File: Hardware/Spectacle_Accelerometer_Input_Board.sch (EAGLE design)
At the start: 45 parts, among them J2 FTDI_DEVICE, J3 AUDIO-JACK3, J4 AUDIO-JACK3, U1 CY8C4146LQI-S422, U2 3.3V/150mA, U3 ADXL345

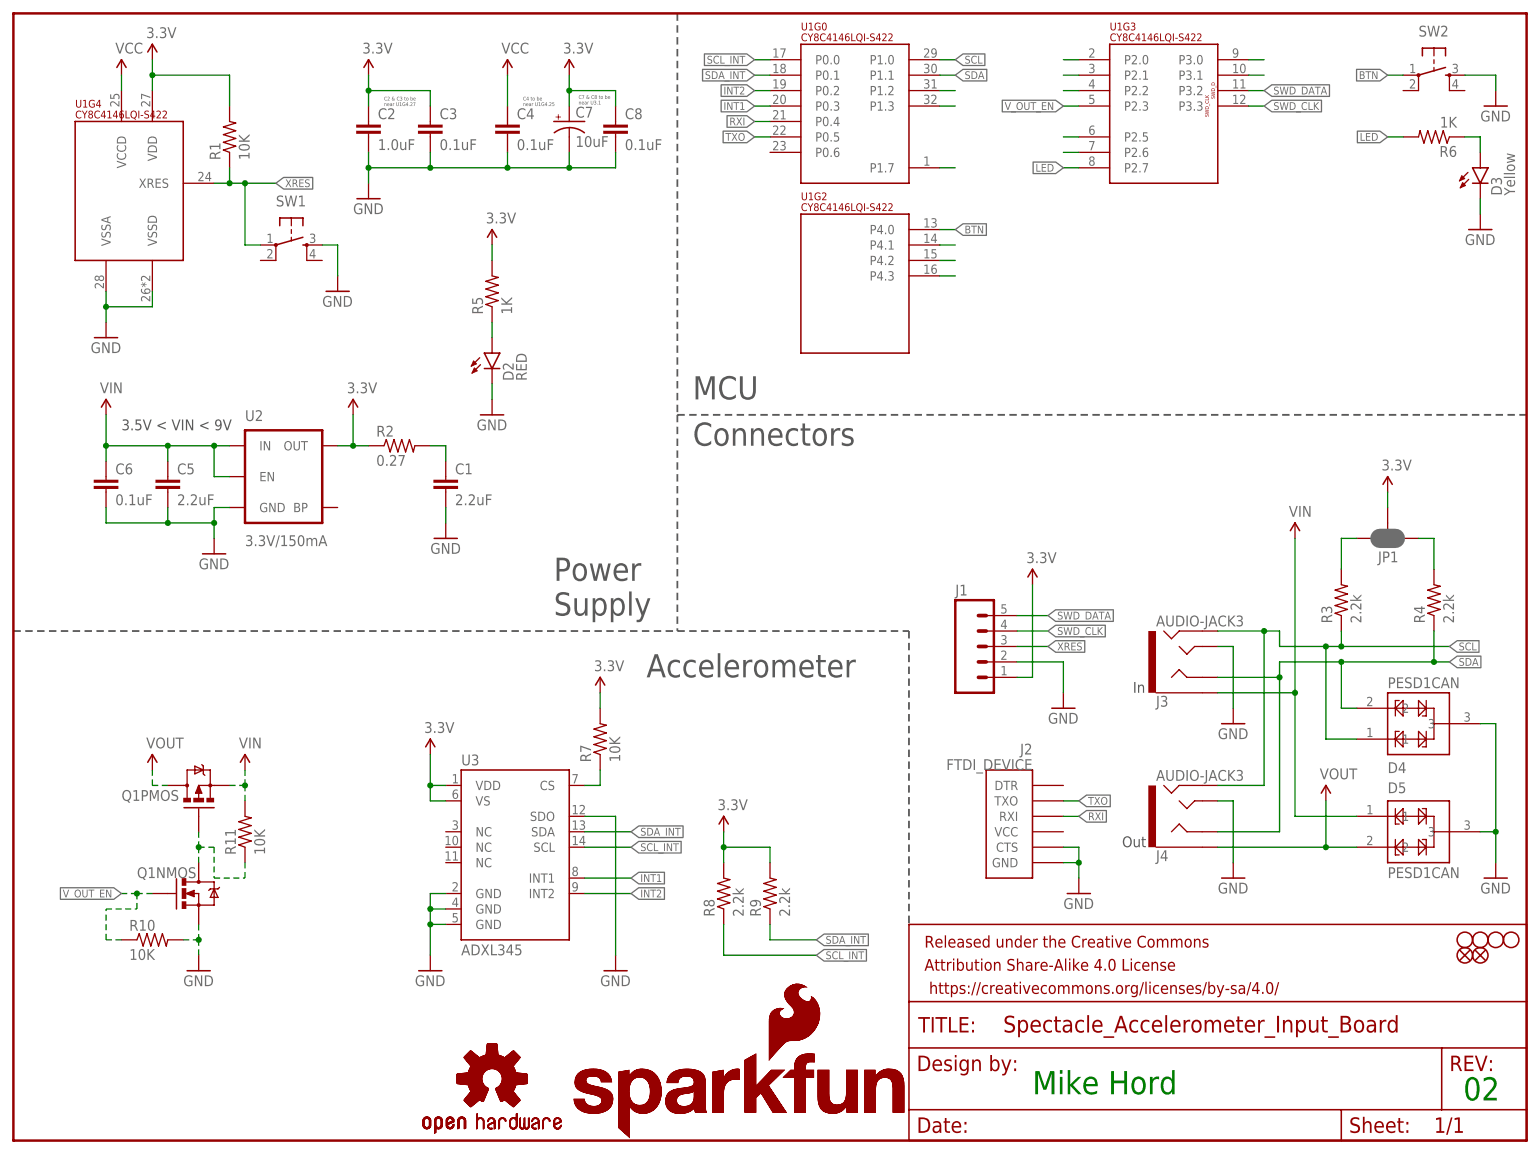
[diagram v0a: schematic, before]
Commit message: I2C disconnect circuitry added
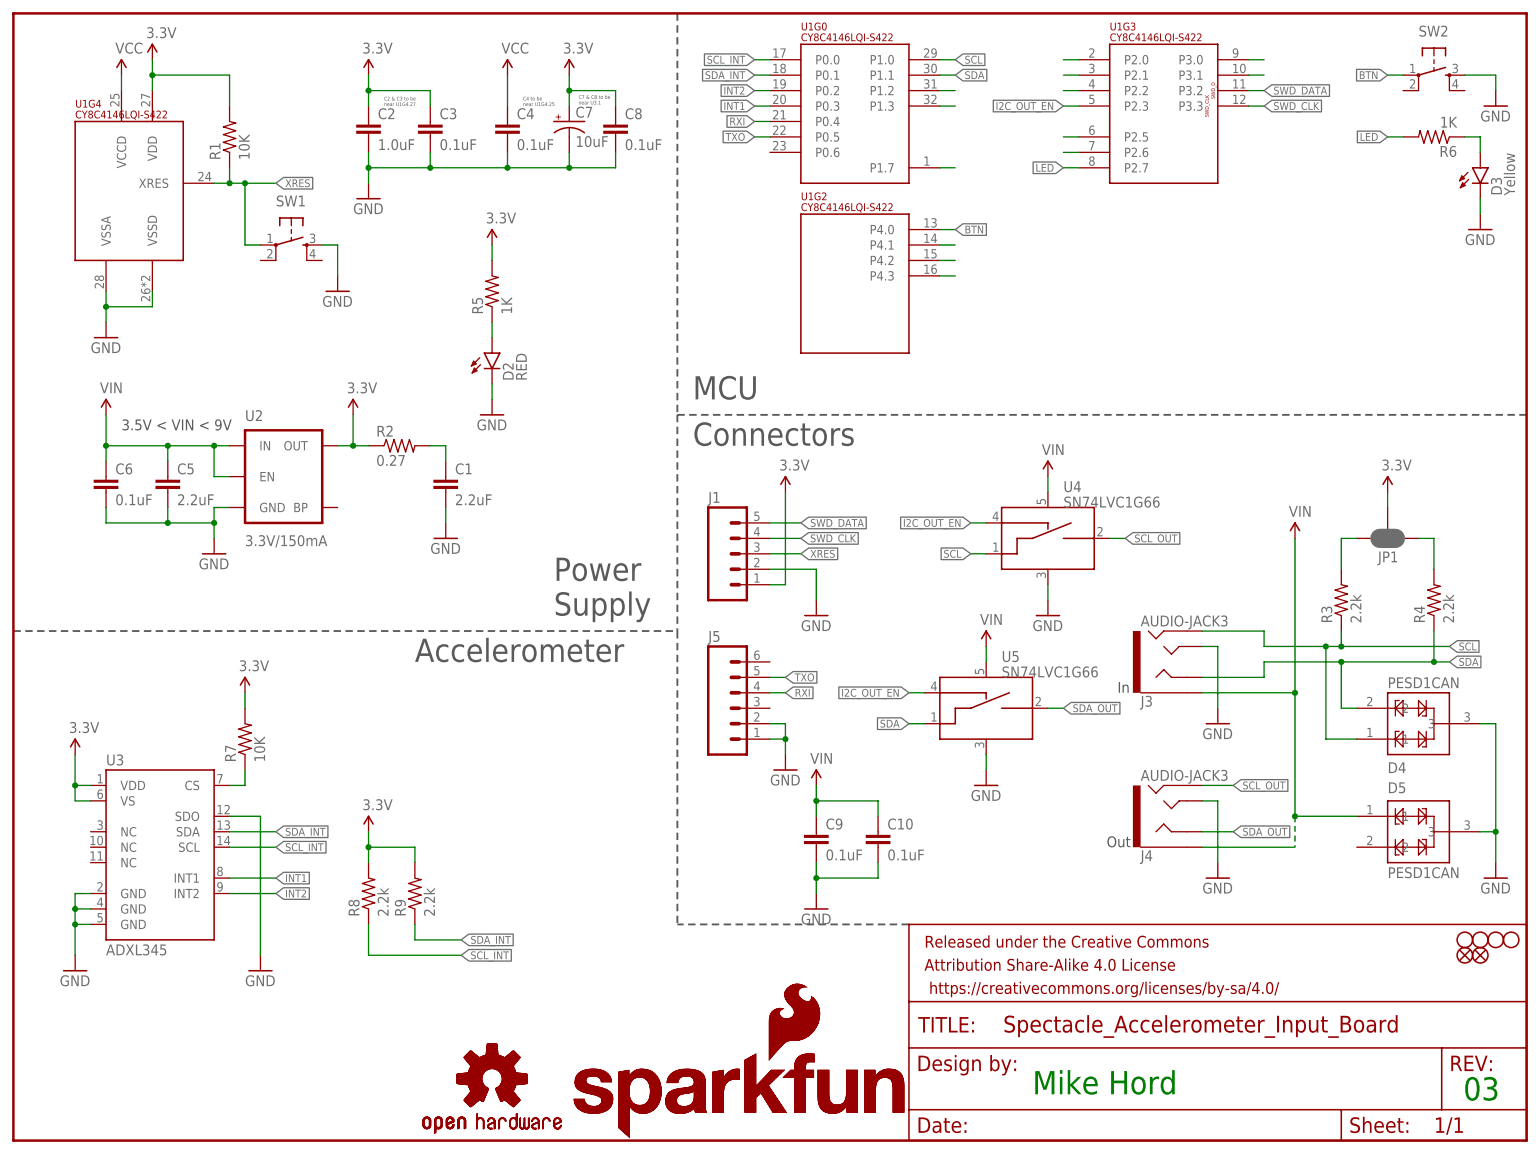
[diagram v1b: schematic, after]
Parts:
- removed J2: FTDI_DEVICE, SparkFun-Connectors:FTDI_DEVICE
- removed Q1: (no value), SparkFun-DiscreteSemi:IRF7509
- removed R10, R11: 10K, SparkFun-Resistors:10KOHM-1/10W-1%(0603)0603
- added C10, C9: 0.1uF, SparkFun-Capacitors:0.1UF-16V(+-10%)(0402)
- added J5: (no value), SparkFun-Connectors:M06NO_SILK_FEMALE_PTH
- added U4, U5: SN74LVC1G66, SparkFun-AnalogIC:SN74LVC1G66_SPST_AMUX
- J1: device SparkFun-Connectors:M05PTH -> SparkFun-Connectors:M05NO_SILK
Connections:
- removed net N$37: Q1NMOS.D, Q1PMOS.G, R11.1
- removed net VOUT: D5.2, J4.EARTH, Q1PMOS.D
- removed net V_OUT_EN: Q1NMOS.G, R10.1, U1G3.P2.3
- new net I2C_OUT_EN: U1G3.P2.3, U4.CTRL_IN, U5.CTRL_IN
- new net SCL_OUT: J4.RING2, U4.A_OUT
- new net SDA_OUT: J4.RING1, U5.A_OUT
- net GND: now also C10.2, C9.2, J5.1, J5.2, U4.VSS, U5.VSS; no longer J2.CTS, J2.GND, Q1NMOS.S, R10.2
- net RXI: now also J5.4; no longer J2.RXI
- net SCL: now also U4.A_IN; no longer J4.RING2
- net SDA: now also U5.A_IN; no longer J4.RING1
- net TXO: now also J5.5; no longer J2.TXO
- net VIN: now also C10.1, C9.1, J4.EARTH, U4.VCC, U5.VCC; no longer Q1PMOS.S, R11.2
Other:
- note added: "03"
- note removed: "02"
- moved on the sheet: J1, J3, J4, R7, R8, R9, U3

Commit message: Change 2.2k I2C pullup to 4.7k Add Arduino test sketch
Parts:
- R3, R4, R8, R9: value 2.2k -> 4.7K; device SparkFun-Resistors:2.2KOHM-1/10W-1%(0603) -> SparkFun-Resistors:4.7KOHM-1/10W-1%(0603)
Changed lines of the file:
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@@
 <grid distance="0.1" unitdist="inch" unit="inch" style="lines" multiple="1" display="no" altdistance="0.01" altunitdist="inch" altunit="inch"/>
 <layers>
-<layer number="1" name="Top" color="4" fill="1" visible="yes" active="no"/>
-<layer number="2" name="Route2" color="1" fill="3" visible="yes" active="no"/>
-<layer number="3" name="Route3" color="4" fill="3" visible="yes" active="no"/>
-<layer number="4" name="Route4" color="1" fill="4" visible="yes" active="no"/>
-<layer number="5" name="Route5" color="4" fill="4" visible="yes" active="no"/>
-<layer number="6" name="Route6" color="1" fill="8" visible="yes" active="no"/>
-<layer number="7" name="Route7" color="4" fill="8" visible="yes" active="no"/>
-<layer number="8" name="Route8" color="1" fill="2" visible="yes" active="no"/>
-<layer number="9" name="Route9" color="4" fill="2" visible="yes" active="no"/>
-<layer number="10" name="Route10" color="1" fill="7" visible="yes" active="no"/>
-<layer number="11" name="Route11" color="4" fill="7" visible="yes" active="no"/>
-<layer number="12" name="Route12" color="1" fill="5" visible="yes" active="no"/>
-<layer number="13" name="Route13" color="4" fill="5" visible="yes" active="no"/>
-<layer number="14" name="Route14" color="1" fill="6" visible="yes" active="no"/>
-<layer number="15" name="Route15" color="4" fill="6" visible="yes" active="no"/>
-<layer number="16" name="Bottom" color="1" fill="1" visible="yes" active="no"/>
-<layer number="17" name="Pads" color="2" fill="1" visible="yes" active="no"/>
-<layer number="18" name="Vias" color="2" fill="1" visible="yes" active="no"/>
-<layer number="19" name="Unrouted" color="6" fill="1" visible="yes" active="no"/>
-<layer number="20" name="Dimension" color="15" fill="1" visible="yes" active="no"/>
-<layer number="21" name="tPlace" color="16" fill="1" visible="yes" active="no"/>
-<layer number="22" name="bPlace" color="14" fill="1" visible="yes" active="no"/>
-<layer number="23" name="tOrigins" color="15" fill="1" visible="yes" active="no"/>
-<layer number="24" name="bOrigins" color="15" fill="1" visible="yes" active="no"/>
-<layer number="25" name="tNames" color="7" fill="1" visible="yes" active="no"/>
-<layer number="26" name="bNames" color="7" fill="1" visible="yes" active="no"/>
-<layer number="27" name="tValues" color="7" fill="1" visible="yes" active="no"/>
-<layer number="28" name="bValues" color="7" fill="1" visible="yes" active="no"/>
+<layer number="1" name="Top" color="4" fill="1" visible="no" active="no"/>
+<layer number="2" name="Route2" color="1" fill="3" visible="no" active="no"/>
+<layer number="3" name="Route3" color="4" fill="3" visible="no" active="no"/>
+<layer number="4" name="Route4" color="1" fill="4" visible="no" active="no"/>
+<layer number="5" name="Route5" color="4" fill="4" visible="no" active="no"/>
+<layer number="6" name="Route6" color="1" fill="8" visible="no" active="no"/>
+<layer number="7" name="Route7" color="4" fill="8" visible="no" active="no"/>
+<layer number="8" name="Route8" color="1" fill="2" visible="no" active="no"/>
+<layer number="9" name="Route9" color="4" fill="2" visible="no" active="no"/>
+<layer number="10" name="Route10" color="1" fill="7" visible="no" active="no"/>
+<layer number="11" name="Route11" color="4" fill="7" visible="no" active="no"/>
+<layer number="12" name="Route12" color="1" fill="5" visible="no" active="no"/>
+<layer number="13" name="Route13" color="4" fill="5" visible="no" active="no"/>
+<layer number="14" name="Route14" color="1" fill="6" visible="no" active="no"/>
+<layer number="15" name="Route15" color="4" fill="6" visible="no" active="no"/>
+<layer number="16" name="Bottom" color="1" fill="1" visible="no" active="no"/>
+<layer number="17" name="Pads" color="2" fill="1" visible="no" active="no"/>
+<layer number="18" name="Vias" color="2" fill="1" visible="no" active="no"/>
+<layer number="19" name="Unrouted" color="6" fill="1" visible="no" active="no"/>
+<layer number="20" name="Dimension" color="15" fill="1" visible="no" active="no"/>
+<layer number="21" name="tPlace" color="16" fill="1" visible="no" active="no"/>
+<layer number="22" name="bPlace" color="14" fill="1" visible="no" active="no"/>
+<layer number="23" name="tOrigins" color="15" fill="1" visible="no" active="no"/>
+<layer number="24" name="bOrigins" color="15" fill="1" visible="no" active="no"/>
+<layer number="25" name="tNames" color="7" fill="1" visible="no" active="no"/>
+<layer number="26" name="bNames" color="7" fill="1" visible="no" active="no"/>
+<layer number="27" name="tValues" color="7" fill="1" visible="no" active="no"/>
+<layer number="28" name="bValues" color="7" fill="1" visible="no" active="no"/>
 <layer number="29" name="tStop" color="7" fill="3" visible="no" active="no"/>
 <layer number="30" name="bStop" color="7" fill="6" visible="no" active="no"/>
@@
 <layer number="35" name="tGlue" color="7" fill="4" visible="no" active="no"/>
 <layer number="36" name="bGlue" color="7" fill="5" visible="no" active="no"/>
-<layer number="37" name="tTest" color="7" fill="1" visible="yes" active="no"/>
-<layer number="38" name="bTest" color="7" fill="1" visible="yes" active="no"/>
+<layer number="37" name="tTest" color="7" fill="1" visible="no" active="no"/>
+<layer number="38" name="bTest" color="7" fill="1" visible="no" active="no"/>
 <layer number="39" name="tKeepout" color="4" fill="11" visible="no" active="no"/>
 <layer number="40" name="bKeepout" color="1" fill="11" visible="no" active="no"/>
@@
 <layer number="44" name="Drills" color="7" fill="1" visible="no" active="no"/>
 <layer number="45" name="Holes" color="7" fill="1" visible="no" active="no"/>
-<layer number="46" name="Milling" color="3" fill="1" visible="yes" active="no"/>
-<layer number="47" name="Measures" color="7" fill="1" visible="yes" active="no"/>
-<layer number="48" name="Document" color="7" fill="1" visible="yes" active="no"/>
-<layer number="49" name="Reference" color="7" fill="1" visible="yes" active="no"/>
-<layer number="50" name="dxf" color="7" fill="1" visible="yes" active="no"/>
-<layer number="51" name="tDocu" color="6" fill="1" visible="yes" active="no"/>
-<layer number="52" name="bDocu" color="7" fill="1" visible="yes" active="no"/>
-<layer number="53" name="tGND_GNDA" color="7" fill="9" visible="yes" active="no"/>
-<layer number="54" name="bGND_GNDA" color="1" fill="9" visible="yes" active="no"/>
-<layer number="56" name="wert" color="7" fill="1" visible="yes" active="no"/>
-<layer number="57" name="tCAD" color="7" fill="1" visible="yes" active="no"/>
-<layer number="59" name="tCarbon" color="7" fill="1" visible="yes" active="no"/>
-<layer number="60" name="bCarbon" color="7" fill="1" visible="yes" active="no"/>
+<layer number="46" name="Milling" color="3" fill="1" visible="no" active="no"/>
+<layer number="47" name="Measures" color="7" fill="1" visible="no" active="no"/>
+<layer number="48" name="Document" color="7" fill="1" visible="no" active="no"/>
+<layer number="49" name="Reference" color="7" fill="1" visible="no" active="no"/>
+<layer number="50" name="dxf" color="7" fill="1" visible="no" active="no"/>
+<layer number="51" name="tDocu" color="6" fill="1" visible="no" active="no"/>
+<layer number="52" name="bDocu" color="7" fill="1" visible="no" active="no"/>
+<layer number="53" name="tGND_GNDA" color="7" fill="9" visible="no" active="no"/>
+<layer number="54" name="bGND_GNDA" color="1" fill="9" visible="no" active="no"/>
+<layer number="56" name="wert" color="7" fill="1" visible="no" active="no"/>
+<layer number="57" name="tCAD" color="7" fill="1" visible="no" active="no"/>
+<layer number="59" name="tCarbon" color="7" fill="1" visible="no" active="no"/>
+<layer number="60" name="bCarbon" color="7" fill="1" visible="no" active="no"/>
 <layer number="90" name="Modules" color="5" fill="1" visible="yes" active="yes"/>
 <layer number="91" name="Nets" color="2" fill="1" visible="yes" active="yes"/>
@@
 <part name="GND9" library="SparkFun-Aesthetics" deviceset="GND" device=""/>
 <part name="SUPPLY7" library="SparkFun-Aesthetics" deviceset="VIN" device=""/>
-<part name="R3" library="SparkFun-Resistors" deviceset="2.2KOHM-1/10W-1%(0603)" device="" value="2.2k"/>
-<part name="R4" library="SparkFun-Resistors" deviceset="2.2KOHM-1/10W-1%(0603)" device="" value="2.2k"/>
+<part name="R3" library="SparkFun-Resistors" deviceset="4.7KOHM-1/10W-1%(0603)" device="" value="4.7K"/>
+<part name="R4" library="SparkFun-Resistors" deviceset="4.7KOHM-1/10W-1%(0603)" device="" value="4.7K"/>
 <part name="JP1" library="SparkFun-Passives" deviceset="JUMPER-PAD-3-NC_BY_PASTE" device=""/>
 <part name="J1" library="SparkFun-Connectors" deviceset="M05" device="NO_SILK"/>
@@
 <part name="C8" library="SparkFun-Capacitors" deviceset="0.1UF-16V(+-10%)(0402)" device="" value="0.1uF"/>
 <part name="SUPPLY14" library="SparkFun-Aesthetics" deviceset="3.3V" device=""/>
-<part name="R8" library="SparkFun-Resistors" deviceset="2.2KOHM-1/10W-1%(0603)" device="" value="2.2k"/>
-<part name="R9" library="SparkFun-Resistors" deviceset="2.2KOHM-1/10W-1%(0603)" device="" value="2.2k"/>
+<part name="R8" library="SparkFun-Resistors" deviceset="4.7KOHM-1/10W-1%(0603)" device="" value="4.7K"/>
+<part name="R9" library="SparkFun-Resistors" deviceset="4.7KOHM-1/10W-1%(0603)" device="" value="4.7K"/>
 <part name="SUPPLY15" library="SparkFun-Aesthetics" deviceset="3.3V" device=""/>
 <part name="H1" library="SparkFun-Electromechanical" deviceset="STAND-OFF" device=""/>

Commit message: Touch-ups for v10 release
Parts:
- J3, J4: value AUDIO-JACK3 -> AUDIO_JACK_TRRSSMD_RA; device SparkFun-Connectors:AUDIO-JACK3 -> SparkFun-Connectors:AUDIO_JACK_TRRSSMD_RA
- J5: device SparkFun-Connectors:M06NO_SILK_FEMALE_PTH -> SparkFun-Connectors:CONN_06NO_SILK_NO_POP
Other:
- note added: "10"
- note removed: "03"
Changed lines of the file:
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@@
 <?xml version="1.0" encoding="utf-8"?>
 <!DOCTYPE eagle SYSTEM "eagle.dtd">
-<eagle version="7.6.0">
+<eagle version="7.7.0">
 <drawing>
 <settings>
@@
 <layer number="255" name="routoute" color="7" fill="1" visible="yes" active="yes"/>
 </layers>
-<schematic xreflabel="%F%N/%S" xrefpart="1_/%S.%C%R">
+<schematic xreflabel="%F%N/%S" xrefpart="/%S.%C%R">
 <attributes>
 </attributes>
@@
 <part name="SUPPLY13" library="SparkFun-Aesthetics" deviceset="3.3V" device=""/>
 <part name="GND3" library="SparkFun-Aesthetics" deviceset="GND" device=""/>
-<part name="J3" library="SparkFun-Connectors" deviceset="AUDIO-JACK3" device=""/>
+<part name="J3" library="SparkFun-Connectors" deviceset="AUDIO_JACK_TRRS" device="SMD_RA"/>
 <part name="D4" library="SparkFun-DiscreteSemi" deviceset="PESD1CAN" device=""/>
 <part name="GND4" library="SparkFun-Aesthetics" deviceset="GND" device=""/>
@@
 <part name="LOGO1" library="SparkFun-Aesthetics" deviceset="SFE_LOGO_NAME_FLAME" device=".1_INCH"/>
 <part name="LOGO2" library="SparkFun-Aesthetics" deviceset="OSHW-LOGO" device="S"/>
-<part name="J4" library="SparkFun-Connectors" deviceset="AUDIO-JACK3" device=""/>
+<part name="J4" library="SparkFun-Connectors" deviceset="AUDIO_JACK_TRRS" device="SMD_RA"/>
 <part name="GND5" library="SparkFun-Aesthetics" deviceset="GND" device=""/>
 <part name="LOGO3" library="SparkFun-Aesthetics" deviceset="OSHW-LOGO" device="S"/>
@@
 <part name="FD1" library="SparkFun-Aesthetics" deviceset="FIDUCIAL" device="UFIDUCIAL"/>
 <part name="FD2" library="SparkFun-Aesthetics" deviceset="FIDUCIAL" device="UFIDUCIAL"/>
-<part name="J5" library="SparkFun-Connectors" deviceset="M06" device="NO_SILK_FEMALE_PTH"/>
+<part name="J5" library="SparkFun-Connectors" deviceset="CONN_06" device="NO_SILK_NO_POP"/>
 <part name="U4" library="SparkFun-AnalogIC" deviceset="SN74LVC1G66_SPST_AMUX" device="" value="SN74LVC1G66"/>
 <part name="U5" library="SparkFun-AnalogIC" deviceset="SN74LVC1G66_SPST_AMUX" device="" value="SN74LVC1G66"/>
@@
 near U3.1</text>
 <text x="167.64" y="7.62" size="3.81" layer="91" font="vector">Mike Hord</text>
-<text x="238.506" y="6.604" size="3.81" layer="91" font="vector">03</text>
+<text x="238.506" y="6.604" size="3.81" layer="91" font="vector">10</text>
 <wire x1="0" y1="83.82" x2="109.22" y2="83.82" width="0.3048" layer="97" style="longdash"/>
 <wire x1="109.22" y1="83.82" x2="109.22" y2="35.56" width="0.3048" layer="97" style="longdash"/>
